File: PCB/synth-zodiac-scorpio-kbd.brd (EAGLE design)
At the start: 76.1 x 72.4 mm, 74 parts, among them U1 74VHC1G125, U13 TL072A, U14 CD40106, U15 40175, U16 CD4051, U18 CD4520, U19 CD4051

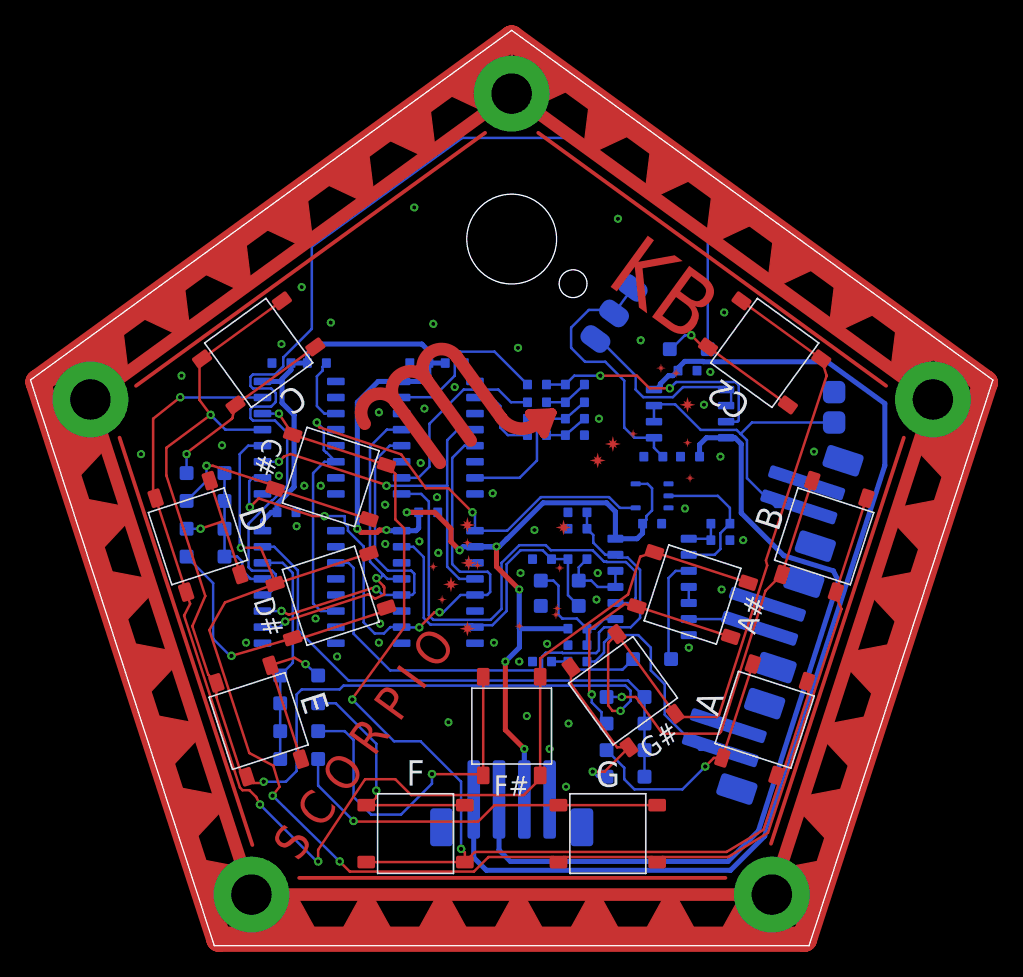
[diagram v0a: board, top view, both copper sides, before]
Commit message: Almost ready for FAB.
Sagittarius was mis-spelled, renamed it.  Taurus is still WIP.
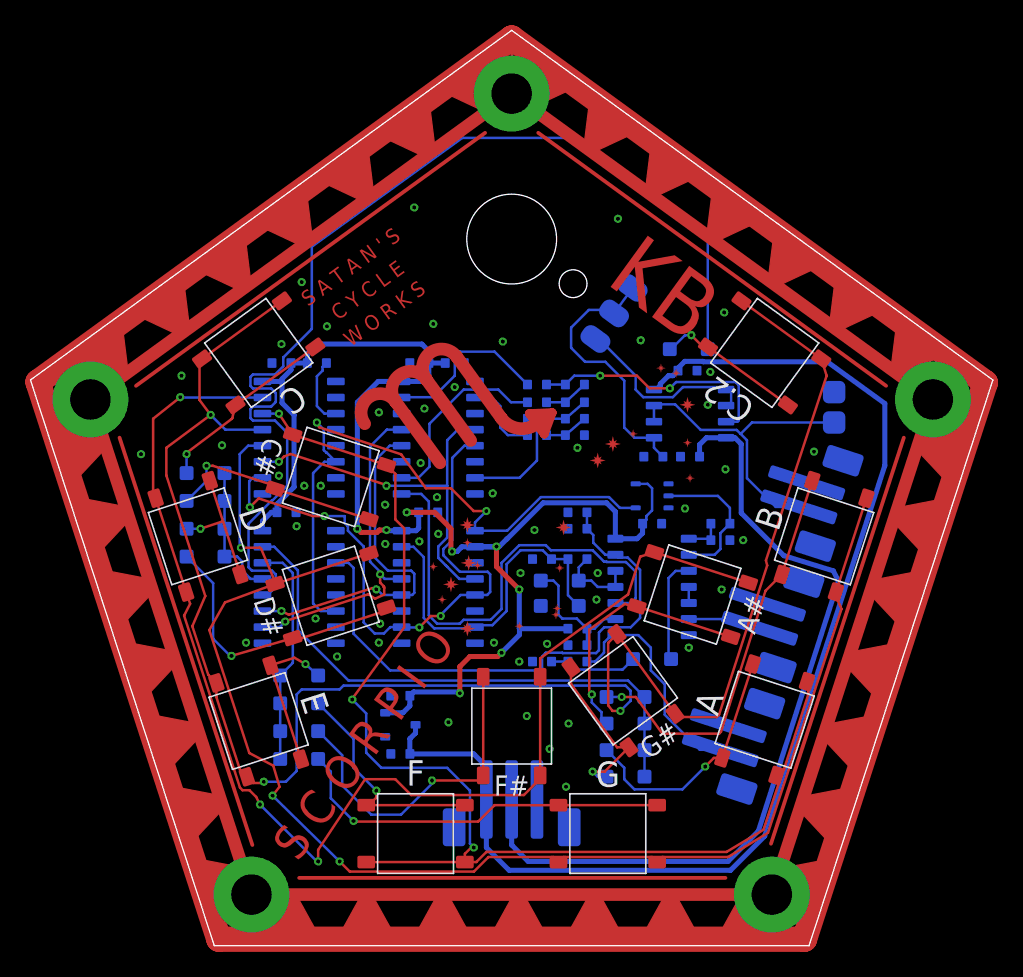
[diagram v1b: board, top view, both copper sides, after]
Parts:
- removed C43: 0.1uF, rlc:0603-CAP
- removed D17, D18, D19, D20: 1N4148, diodes:SOD-123
- added C.2: Tact. Sw., switch-smd:B3FS
- added C5, C6: 1uF, rlc:0603-CAP
- added D1, D2, D3, D4: 1N4148, diodes:SOD-123
- added VR: 5V, regulators:SOT-23
- C2: value Tact. Sw. -> 0.1uF; device switch-smd:B3FS -> rlc:0603-CAP
- PWR: value (none) -> JST, 3P, VT, SMT; device con-jst:B4B-PH-SM4 -> con-jst:B3B-PH-SM4
- moved C2 38.2 mm to (19.8, 46.7), flipped to the bottom, turned to 0 degrees
- moved D16 34.2 mm to (52.0, 47.8)
- moved D5 28.7 mm to (13.8, 35.8)
- moved D7 28.3 mm to (13.8, 31.4)
- moved D8 27.9 mm to (21.2, 22.0), turned to 180 degrees
- moved D12 27.0 mm to (47.0, 14.0), turned to 0 degrees
- moved D15 26.3 mm to (47.0, 20.3), turned to 0 degrees
- moved D13 26.1 mm to (47.0, 16.1), turned to 0 degrees
- moved D14 25.8 mm to (47.0, 18.2), turned to 0 degrees
- moved D10 17.6 mm to (21.2, 17.6), turned to 180 degrees
- moved D11 17.6 mm to (21.2, 15.4), turned to 180 degrees
- moved D9 17.6 mm to (21.2, 19.8), turned to 180 degrees
- moved D6 4.40 mm to (13.8, 33.6)
- renumbered C44 to C3, C45 to C1, C46 to C12, C47 to C13, C48 to C14, C49 to C11, C50 to C15, C51 to C7, C52 to C8, C53 to C9, C54 to C10, C59 to C4, GATE to GATE2EG, KB_CV to KB2VCO, R57 to R2, R74 to R5, R75 to R1, R76 to R3, R77 to R6, R78 to R7, R79 to R4, R80 to R8, R81 to R9, R82 to R10, R83 to R11, R84 to R15, R85 to R14, R86 to R13, R87 to R12, TRIG to TRIG2EG, U13 to U7, U14 to U6, U15 to U5, U16 to U3, U18 to U2, U19 to U4
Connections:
- net +5V: now also C2.1, C6.1, VR.2; no longer C43.1, PWR.3
- net +9V: now also C5.1, VR.3
- net C0: now also C.2.1, C.2.2; no longer C2.1, C2.2
- net GND: now also C2.2, C5.2, C6.2, D2.A, PWR.3, VR.1; no longer C43.2, D7.A, PWR.4
- net MR: now also D2.K; no longer D7.K
- net N$102: now also D1.A; no longer D5.A
- net N$112: now also D1.K; no longer D5.K
- net N$114: now also D3.K; no longer D8.K
- net N$115: now also D3.A; no longer D8.A
- net N$120: now also D4.A; no longer D6.A
- net N$122: now also D5.A; no longer D9.A
- net N$123: now also D6.A; no longer D10.A
- net N$124: now also D7.A; no longer D11.A
- net N$125: now also D8.A; no longer D12.A
- net N$126: now also D9.A; no longer D13.A
- net N$127: now also D10.A; no longer D14.A
- net N$128: now also D11.A; no longer D15.A
- net N$129: now also D12.A; no longer D16.A
- net N$130: now also D13.A; no longer D17.A
- net N$131: now also D14.A; no longer D18.A
- net N$132: now also D15.A; no longer D19.A
- net N$133: now also C.2.3, C.2.4, D16.A; no longer C2.3, C2.4, D20.A
- net R0: now also D4.K, D5.K, D7.K; no longer D10.K, D11.K, D9.K
- net R1: now also D10.K, D11.K, D8.K, D9.K; no longer D12.K, D13.K, D14.K, D15.K
- net R2: now also D12.K, D13.K, D14.K, D15.K; no longer D16.K, D17.K, D18.K, D19.K
- net R3: now also D16.K; no longer D20.K
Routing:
- net +9V: track 85.3 -> 95.4 mm
- net C1: track 94.2 -> 96.7 mm
- net N$127: track 28.0 -> 26.4 mm
- net KB_CLK: track 49.0 -> 50.4 mm
- net +5V: track 113.4 -> 114.8 mm
- net -9V: track 66.5 -> 65.3 mm
- net N$126: track 19.0 -> 18.2 mm
- net N$110: track 47.4 -> 48.0 mm
- net N$109: track 30.4 -> 31.0 mm
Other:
- board text added: "S A T A N ' S C Y C L E W O R K S"
